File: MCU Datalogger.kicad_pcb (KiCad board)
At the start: 2 copper layers, 0 parts

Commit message: Setup PCBNew.
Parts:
- added BT1: Battery, Connector_PinHeader_2.54mm:PinHeader_1x02_P2.54mm_Vertical, F.Cu at (122.5, 108.7)
- added C1: 0.1uF, Capacitor_SMD:C_0805_2012Metric, F.Cu at (144.8, 98.4)
- added C2: 22pF, Capacitor_SMD:C_0805_2012Metric, F.Cu at (144.8, 101.4)
- added C3: 22pF, Capacitor_SMD:C_0805_2012Metric, F.Cu at (144.8, 104.4)
- added C4: 0.1uF, Capacitor_SMD:C_0805_2012Metric, F.Cu at (144.8, 107.4)
- added C6: 100nF, Capacitor_SMD:C_0805_2012Metric, F.Cu at (144.8, 110.4)
- added D1: LED, LED_SMD:LED_0805_2012Metric, F.Cu at (149.3, 98.4)
- added D2: LED, LED_SMD:LED_0805_2012Metric, F.Cu at (149.3, 101.4)
- added H1: MountingHole, MountingHole:MountingHole_2.1mm, F.Cu at (123.1, 86.2)
- added H2: MountingHole, MountingHole:MountingHole_2.1mm, F.Cu at (123.1, 92.0)
- added H3: MountingHole, MountingHole:MountingHole_2.1mm, F.Cu at (123.1, 97.7)
- added H4: MountingHole, MountingHole:MountingHole_2.1mm, F.Cu at (123.1, 103.5)
- added J1: Conn_01x04_Pin, Connector_PinHeader_2.54mm:PinHeader_1x04_P2.54mm_Vertical, F.Cu at (160.5, 85.7)
- added J2: Conn_01x04_Pin, Connector_PinHeader_2.54mm:PinHeader_1x04_P2.54mm_Vertical, F.Cu at (165.1, 85.7)
- added J3: Conn_01x09_Pin, Connector_PinHeader_2.54mm:PinHeader_1x09_P2.54mm_Vertical, F.Cu at (155.8, 85.7)
- added J4: Conn_02x03_Odd_Even, Connector_PinHeader_2.54mm:PinHeader_2x03_P2.54mm_Vertical, F.Cu at (160.5, 97.9)
- added R1: 4.7k, Resistor_SMD:R_0805_2012Metric, F.Cu at (128.2, 84.8)
- added R2: 10k, Resistor_SMD:R_0805_2012Metric, F.Cu at (128.2, 87.8)
- added R3: 10k, Resistor_SMD:R_0805_2012Metric, F.Cu at (128.2, 90.7)
- added R4: 330, Resistor_SMD:R_0805_2012Metric, F.Cu at (128.2, 93.7)
- added R5: 330, Resistor_SMD:R_0805_2012Metric, F.Cu at (128.2, 96.6)
- added R6: 10k, Resistor_SMD:R_0805_2012Metric, F.Cu at (128.2, 99.6)
- added R7: 4.7k, Resistor_SMD:R_0805_2012Metric, F.Cu at (128.2, 102.5)
- added U1: 24LC1025, Package_SO:SOIC-8_5.23x5.23mm_P1.27mm, F.Cu at (135.5, 86.7)
- added U2: 24LC1025, Package_SO:SOIC-8_5.23x5.23mm_P1.27mm, F.Cu at (135.5, 93.5)
- added U3: DS1337S_, Footprints:SOIC127P600X175-8N, F.Cu at (135.5, 111.5)
- added U4: ATMEGA328P-AU, Footprints:QFP80P900X900X120-32N, F.Cu at (136.9, 102.6)
- added Y1: 16 MHz, Crystal:Crystal_SMD_5032-2Pin_5.0x3.2mm_HandSoldering, F.Cu at (145.8, 85.8)
- added Y2: 32.768 KHz, Crystal:Crystal_SMD_5032-2Pin_5.0x3.2mm_HandSoldering, F.Cu at (145.8, 90.6)

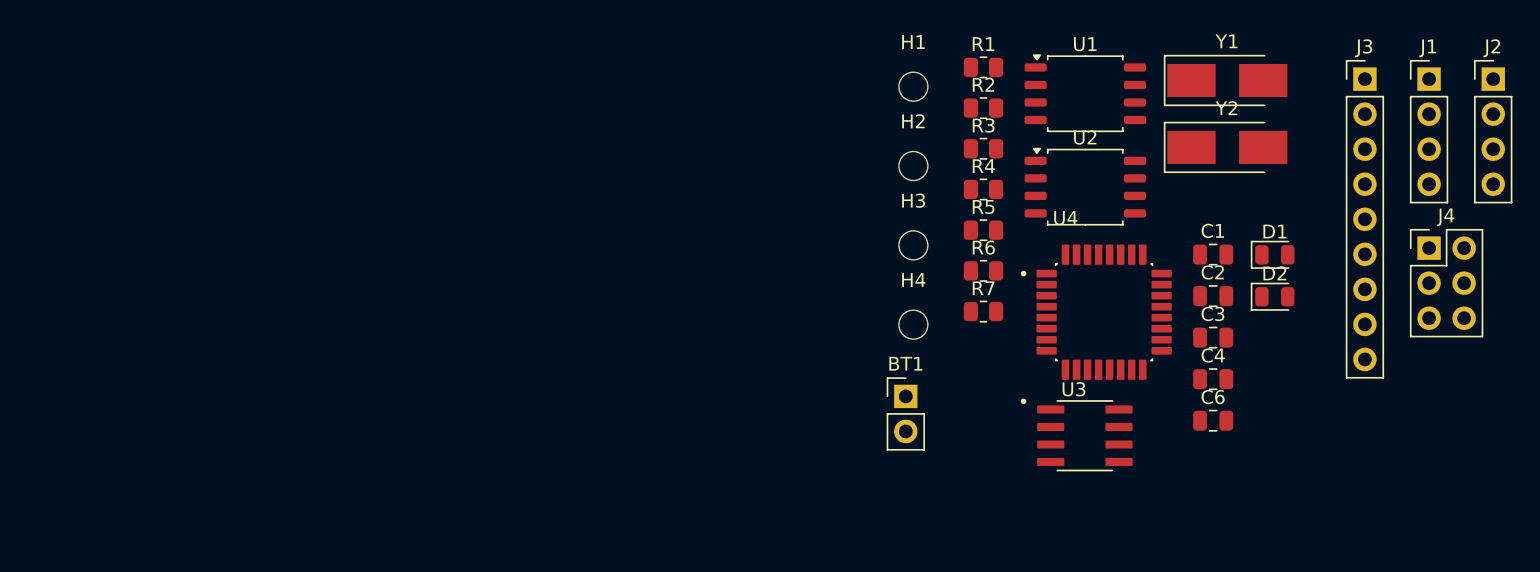
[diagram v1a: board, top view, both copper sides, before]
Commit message: Completed placement of footprints in PCBNew.
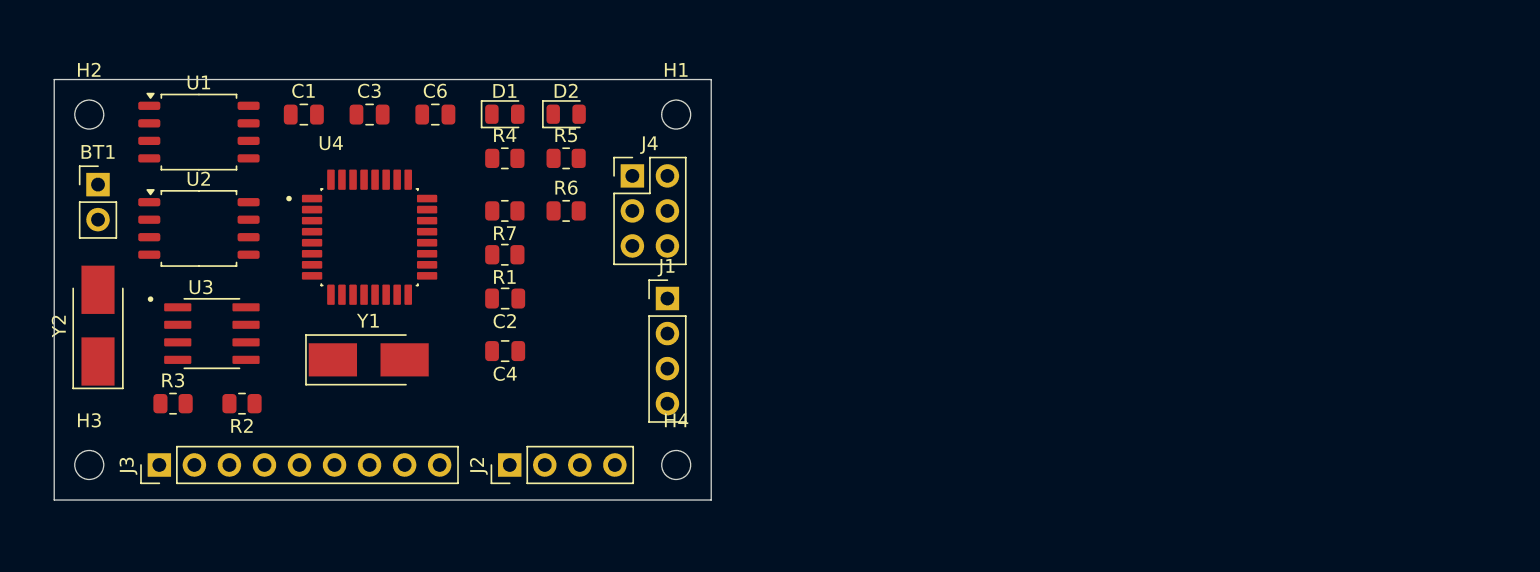
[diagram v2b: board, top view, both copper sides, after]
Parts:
- moved J3 91.8 mm to (68.4, 113.6), turned to 90 degrees
- moved Y2 82.9 mm to (64.0, 103.5), turned to 90 degrees
- moved J2 76.6 mm to (93.8, 113.6), turned to 90 degrees
- moved C1 66.7 mm to (78.9, 88.2)
- moved Y1 65.5 mm to (83.6, 106.0)
- moved U2 64.3 mm to (71.3, 96.5)
- moved U1 64.3 mm to (71.3, 89.5)
- moved U3 63.7 mm to (72.2, 104.1)
- moved C3 63.3 mm to (83.7, 88.2)
- moved H3 61.8 mm to (63.3, 113.6)
- moved R3 61.6 mm to (69.4, 109.2)
- moved C6 60.6 mm to (88.4, 88.2)
- moved BT1 60.5 mm to (64.0, 93.3)
- moved H2 59.9 mm to (63.3, 88.2)
- moved J4 58.0 mm to (102.7, 92.7)
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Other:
- board outline added: 47.6 x 30.5 mm

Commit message: Routing except GND and Vcc complete + changed edge cuts surrounding mounting holes.
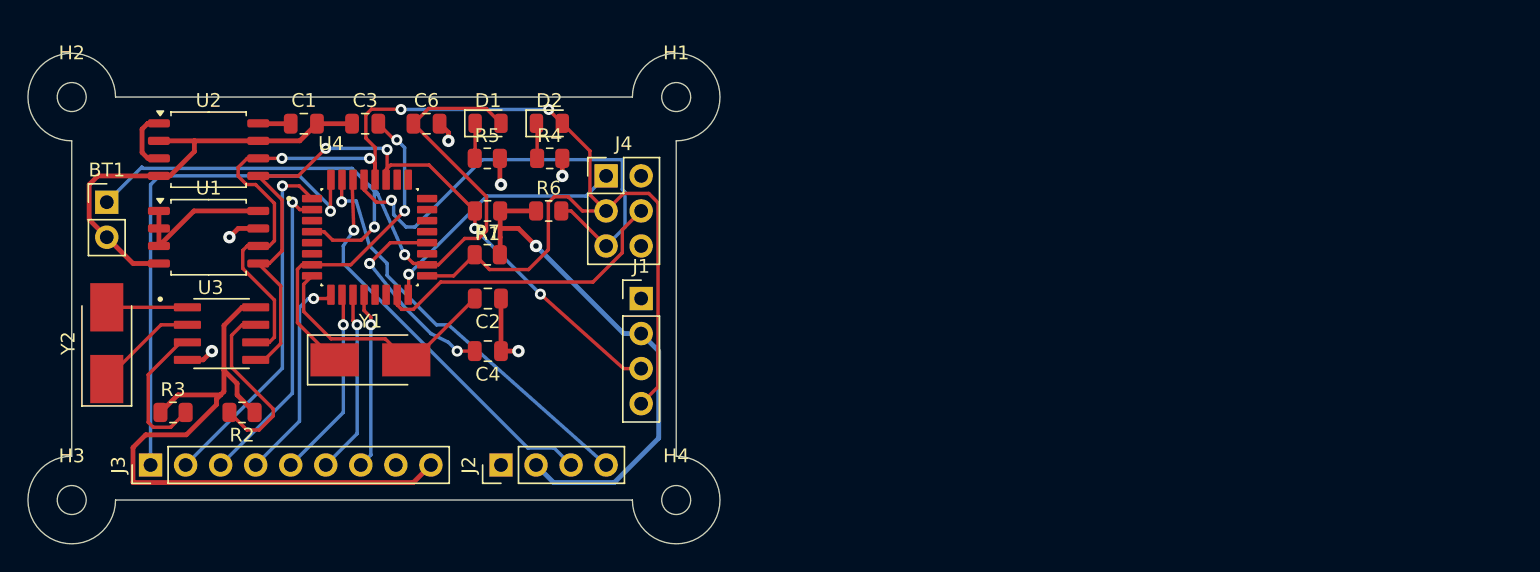
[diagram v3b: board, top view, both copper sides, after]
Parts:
- moved U1 7.65 mm to (72.0, 97.1)
- moved U2 5.76 mm to (72.0, 90.8)
- moved R5 5.72 mm to (92.2, 91.4)
- moved R7 3.42 mm to (92.2, 98.4), turned to 0 degrees
- moved R1 3.41 mm to (92.2, 95.2)
- moved R4 3.25 mm to (96.7, 91.4)
- moved H3 2.84 mm to (62.1, 116.2)
- moved H4 2.54 mm to (105.9, 116.2)
- moved J1 1.91 mm to (103.3, 101.6)
- moved J4 1.90 mm to (100.8, 92.7)
- moved H2 1.80 mm to (62.1, 87.0)
- moved BT1 1.42 mm to (64.6, 94.6)
- moved Y2 1.42 mm to (64.6, 104.8)
- moved D1 1.38 mm to (92.2, 88.9)
- moved D2 1.38 mm to (96.7, 88.9)
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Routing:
- net /Vcc: track 0.00 -> 105.7 mm, vias 0 -> 1
- net /SCK: track 0.00 -> 95.4 mm, vias 0 -> 4
- net Net-(BT1-+): track 0.00 -> 59.4 mm, vias 0 -> 2
- net /SDA: track 0.00 -> 55.5 mm, vias 0 -> 4
- net GND: track 0.00 -> 47.0 mm, vias 0 -> 6
- net /D2: track 0.00 -> 37.2 mm, vias 0 -> 1
- net /RESET: track 0.00 -> 34.4 mm, vias 0 -> 1
- net /TX: track 0.00 -> 30.0 mm, vias 0 -> 1
- net /RX: track 0.00 -> 28.9 mm, vias 0 -> 1
- net /D3: track 0.00 -> 25.7 mm, vias 0 -> 1
- net Net-(U4-PB6): track 0.00 -> 24.4 mm, vias 0 -> 2
- net /D4: track 0.00 -> 22.9 mm, vias 0 -> 1
- net /MOSI: track 0.00 -> 22.5 mm
- net /MISO: track 0.00 -> 18.8 mm, vias 0 -> 1
- net Net-(U4-PB7): track 0.00 -> 18.5 mm
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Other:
- board size 47.6 x 30.5 mm -> 50.2 x 35.6 mm

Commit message: Refined routing complete.
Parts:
- moved D2 0.05 mm to (96.7, 88.9)
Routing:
- net GND: track 47.0 -> 170.3 mm, vias 6 -> 8
- net /Vcc: track 105.7 -> 119.5 mm, vias 1 -> 5
- net Net-(BT1-+): track 59.4 -> 57.2 mm
- net /RX: track 28.9 -> 28.0 mm
- added copper zone on B.Cu, net /Vcc
- added copper zone on B.Cu, net GND

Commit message: Fixed outstanding issues and set Silkscreen.
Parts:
- added REF**: KiCad-Logo2_5mm_SilkScreen, Symbol:KiCad-Logo2_5mm_SilkScreen, B.Cu at (83.8, 92.6)
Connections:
- BT1 pad 1: Net-(BT1-+) -> /Vcc
- C6 pad 1: Net-(BT1-+) -> /Vcc
- D1 pad 2: Net-(BT1-+) -> /Vcc
- U4 pad 18: Net-(BT1-+) -> /Vcc
- U4 pad 4: Net-(BT1-+) -> /Vcc
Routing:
- net /Vcc: track 119.5 -> 180.4 mm, vias 5 -> 8
- net Net-(BT1-+): track 57.2 -> 0.00 mm, vias 2 -> 0
- net /SCK: track 95.4 -> 99.3 mm
- net /D3: track 25.7 -> 25.1 mm
- net GND: vias 8 -> 6
- removed copper zone on B.Cu, net GND
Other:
- board text added: "- 2Mb EEPROM - RTC - I2C, SPI, GPIOs"
- board text added: "2"
- board text added: "3"
- board text added: "4"
- board text added: "5"
- board text added: "6"
- board text added: "7"
- board text added: "8"
- board text added: "Data Logger with the ATMega328P"
- board text added: "Designed by Jack Tanner (520) 307-5172"
- board text added: "GND"
- board text added: "I2C"
- board text added: "ICSP"
- board text added: "MISO | Vcc SCK | MOSI RESET| GND"
- board text added: "RX"
- board text added: "SCK"
- board text added: "SDA"
- board text added: "Serial"
- board text added: "TX"
- board text added: "Vcc"

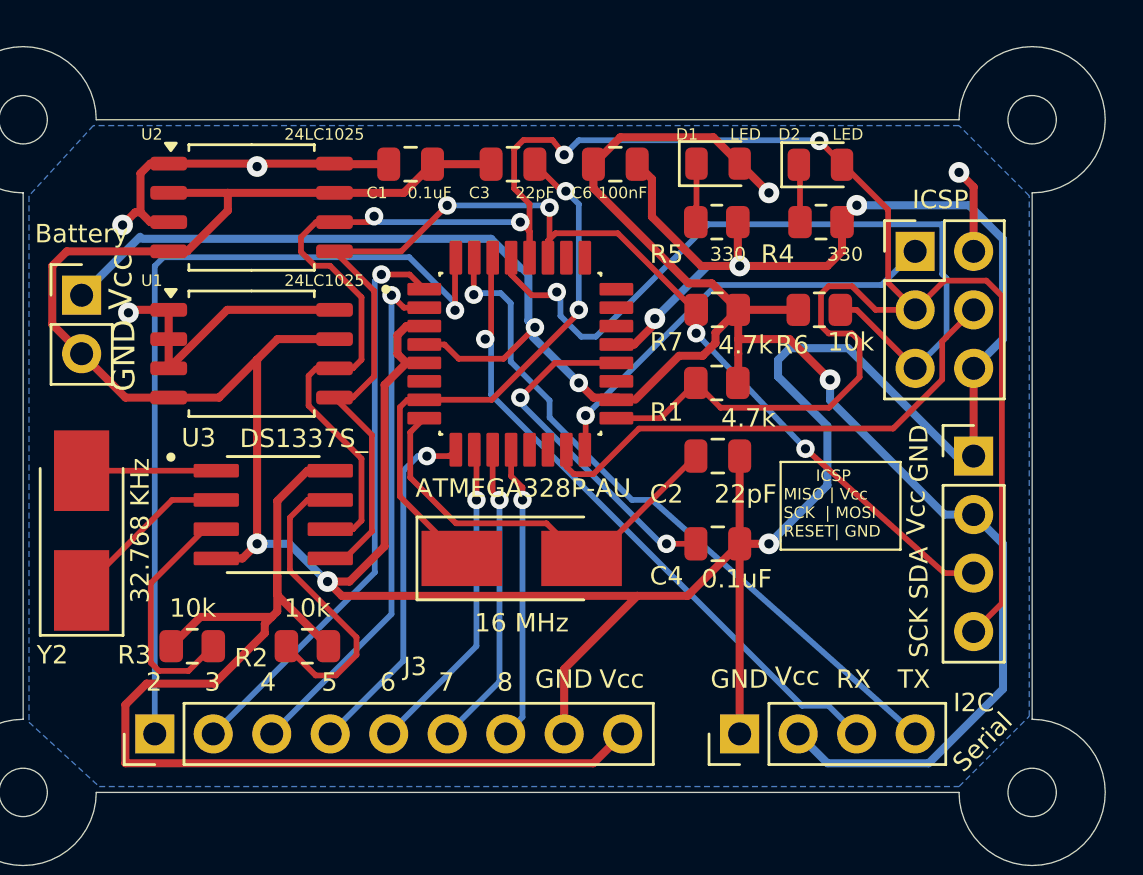
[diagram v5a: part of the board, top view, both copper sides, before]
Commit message: Fixed 2 layer PCB regarding SCL/SCK issues.
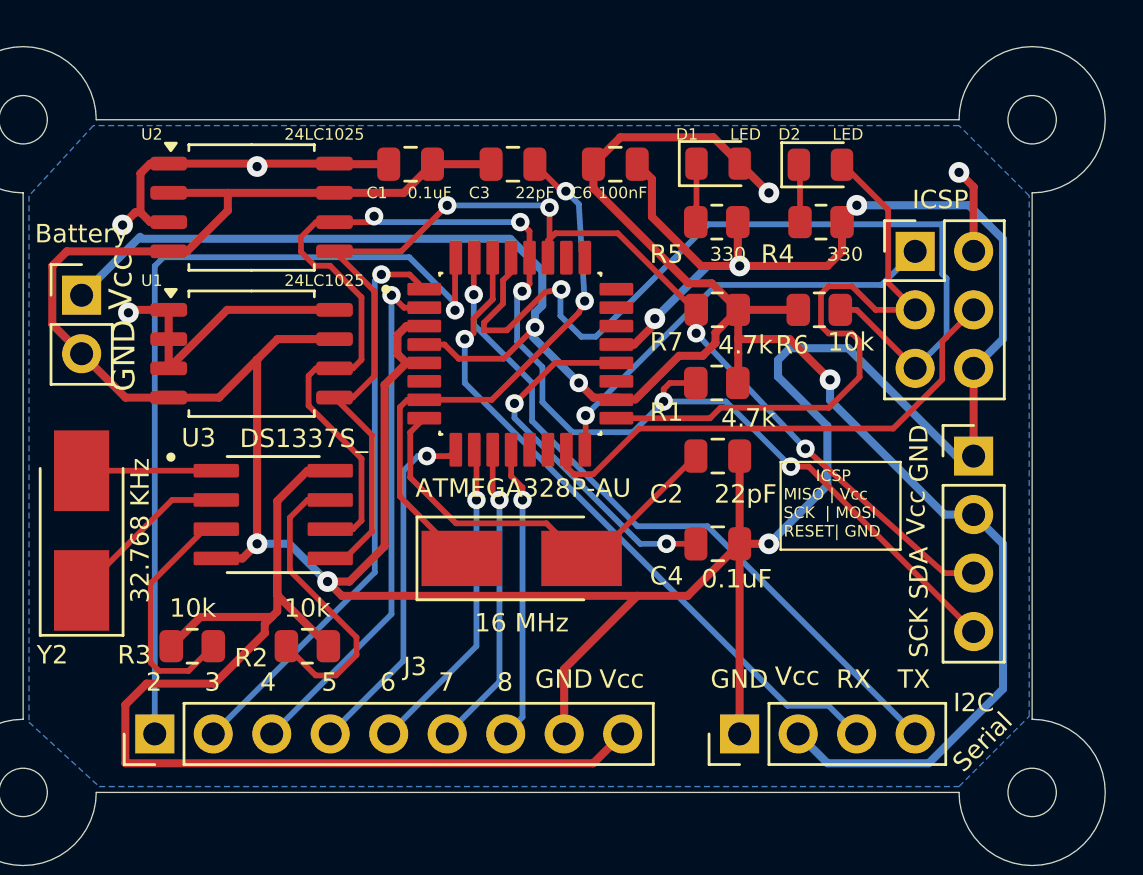
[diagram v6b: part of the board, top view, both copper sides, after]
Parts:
- removed REF**: KiCad-Logo2_5mm_SilkScreen, Symbol:KiCad-Logo2_5mm_SilkScreen
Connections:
- J1 pad 4: /SCK -> /SCL
- R7 pad 1: /SCK -> /SCL
- U1 pad 6: /SCK -> /SCL
- U2 pad 6: /SCK -> /SCL
- U3 pad 6: /SCK -> /SCL
- U4 pad 28: /SCK -> /SCL
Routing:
- net /SCK: track 99.3 -> 28.5 mm, vias 4 -> 0
- net /SCL: track 0.00 -> 62.8 mm, vias 0 -> 5
- net /RESET: track 34.4 -> 39.0 mm
- net /RX: track 28.2 -> 29.3 mm
- net /Vcc: track 180.4 -> 181.1 mm
- net Net-(U4-AREF): track 15.2 -> 15.9 mm

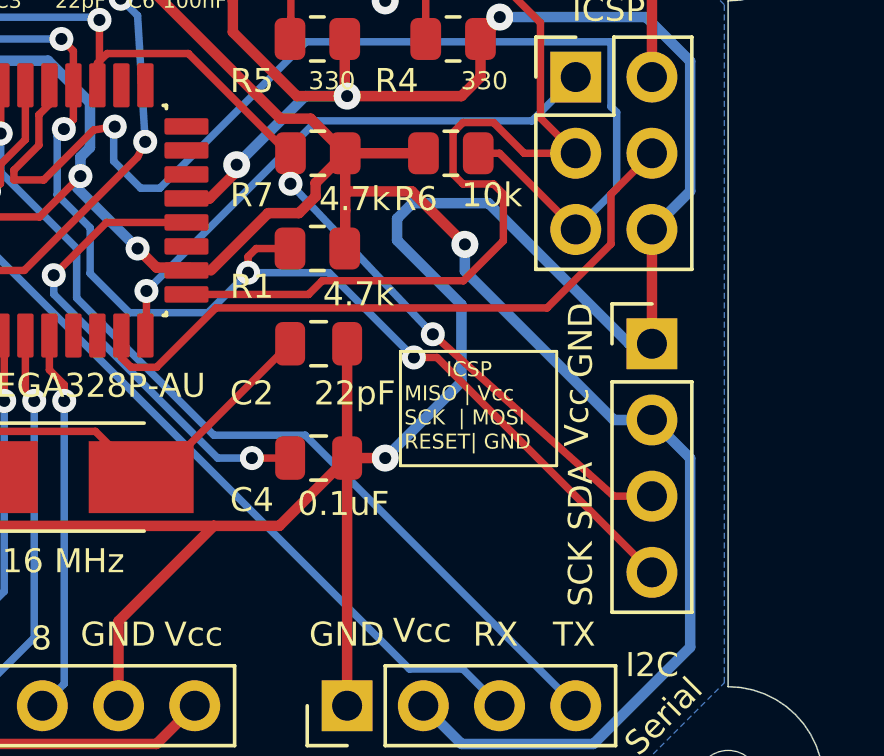
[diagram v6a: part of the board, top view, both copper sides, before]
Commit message: Completed 2-Layer PCB Project.
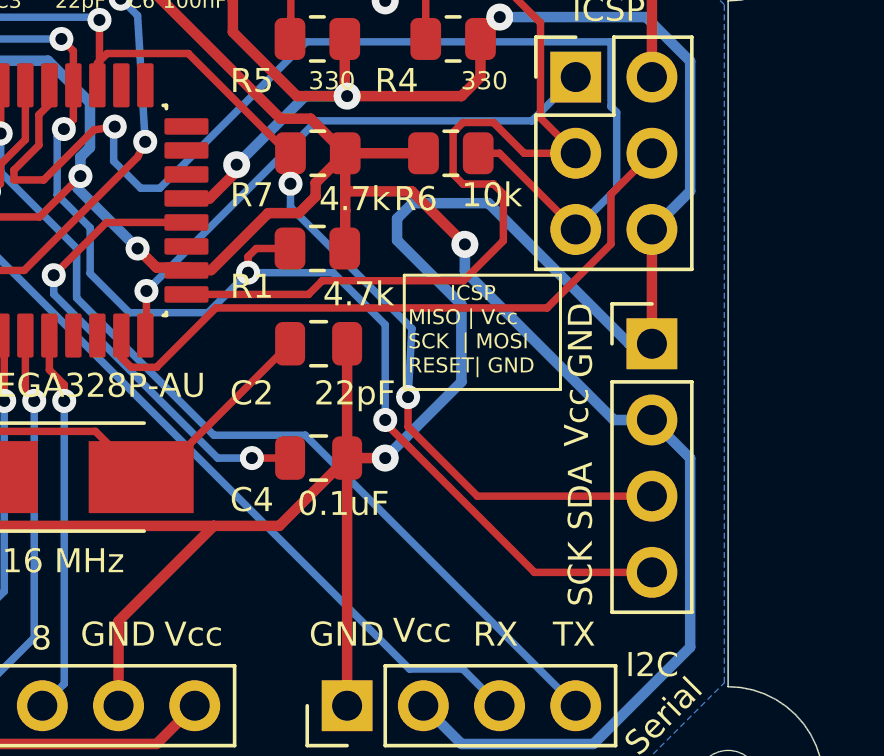
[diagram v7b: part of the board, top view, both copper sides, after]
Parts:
- added REF**: KiCad-Logo2_5mm_SilkScreen, Symbol:KiCad-Logo2_5mm_SilkScreen, B.Cu at (83.7, 92.2)
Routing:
- net /SDA: track 55.9 -> 58.5 mm
- net /SCL: track 62.8 -> 64.7 mm
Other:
- board text added: "0.2000 mm / 0.0000 mm"
- board text added: "0.3000 mm"
- board text added: "1.6000 mm"
- board text added: "50.1600 mm x 35.5550 mm"
- board text added: "BOARD CHARACTERISTICS"
- board text added: "Board Thickness:"
- board text added: "Board overall dimensions:"
- board text added: "Castellated pads:"
- board text added: "Copper Finish:"
- board text added: "Copper Layer Count:"
- board text added: "Edge card connectors:"
- board text added: "Impedance Control:"
- board text added: "Min hole diameter:"
- board text added: "Min track/spacing:"
- board text added: "No"
- board text added: "None"
- board text added: "Plated Board Edge:"
